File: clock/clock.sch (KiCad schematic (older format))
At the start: 3 parts, among them P101 CONN_01X03, P102 CONN_FAN_PWM, P103 XG4A-1631

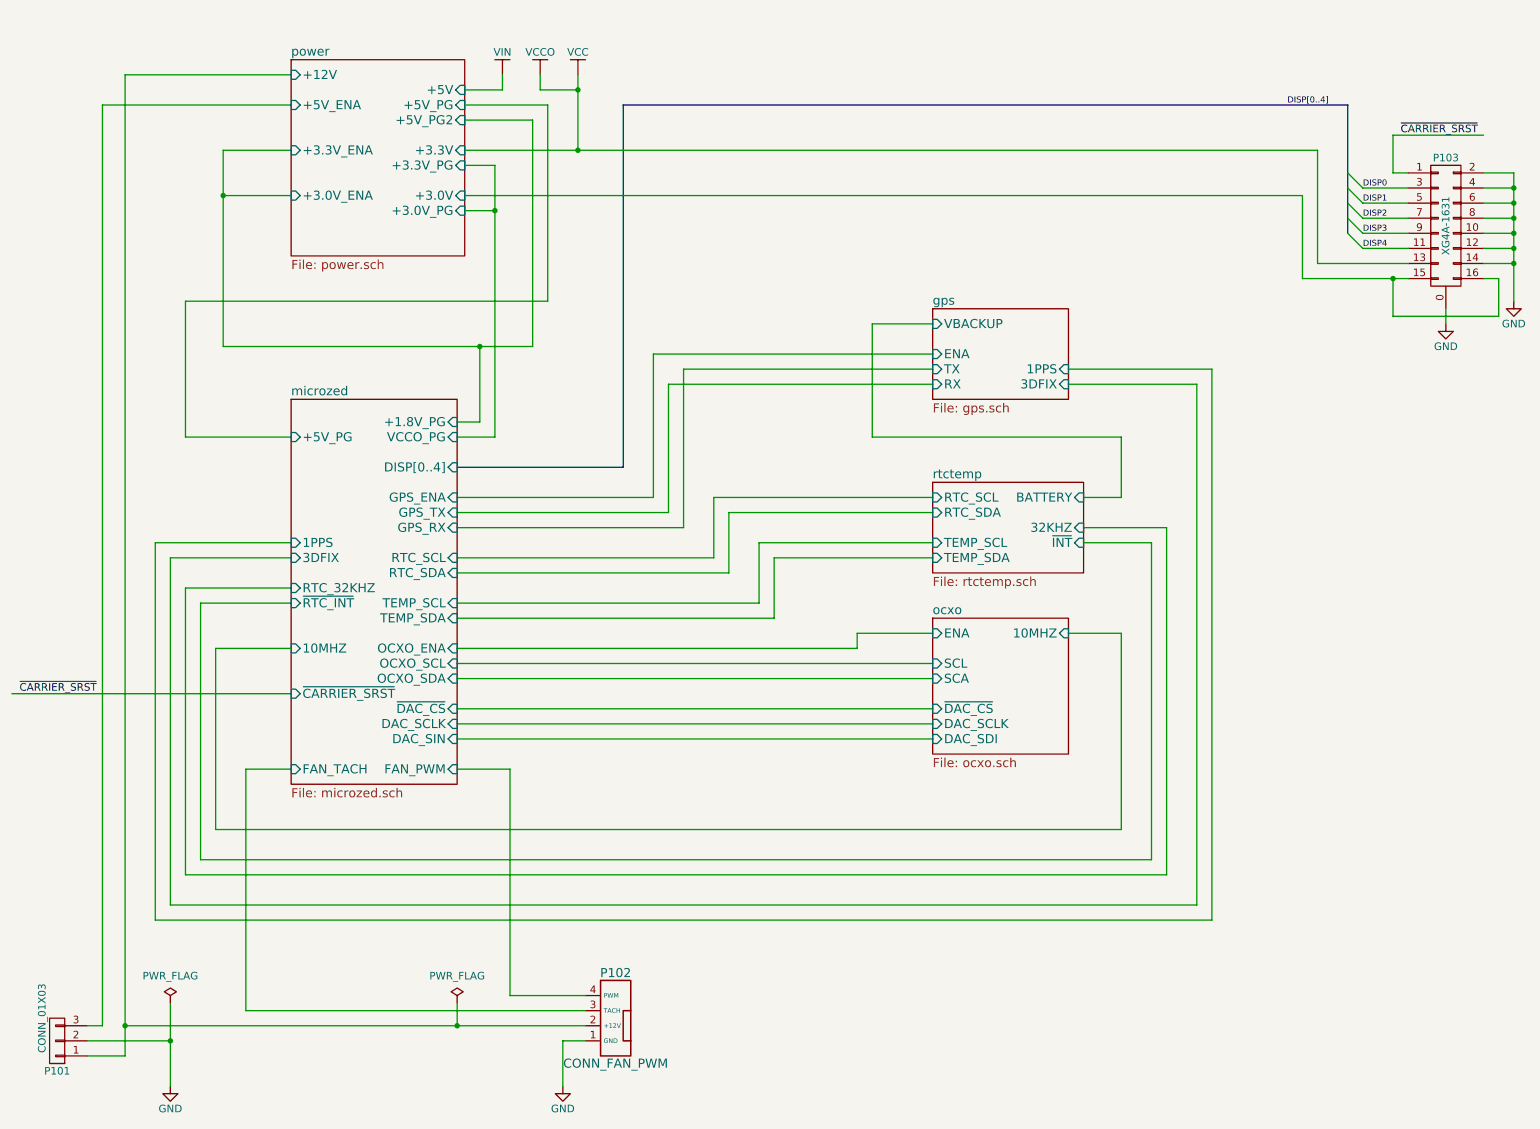
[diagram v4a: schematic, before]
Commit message: Connect temperature sensor interrupt to FPGA.
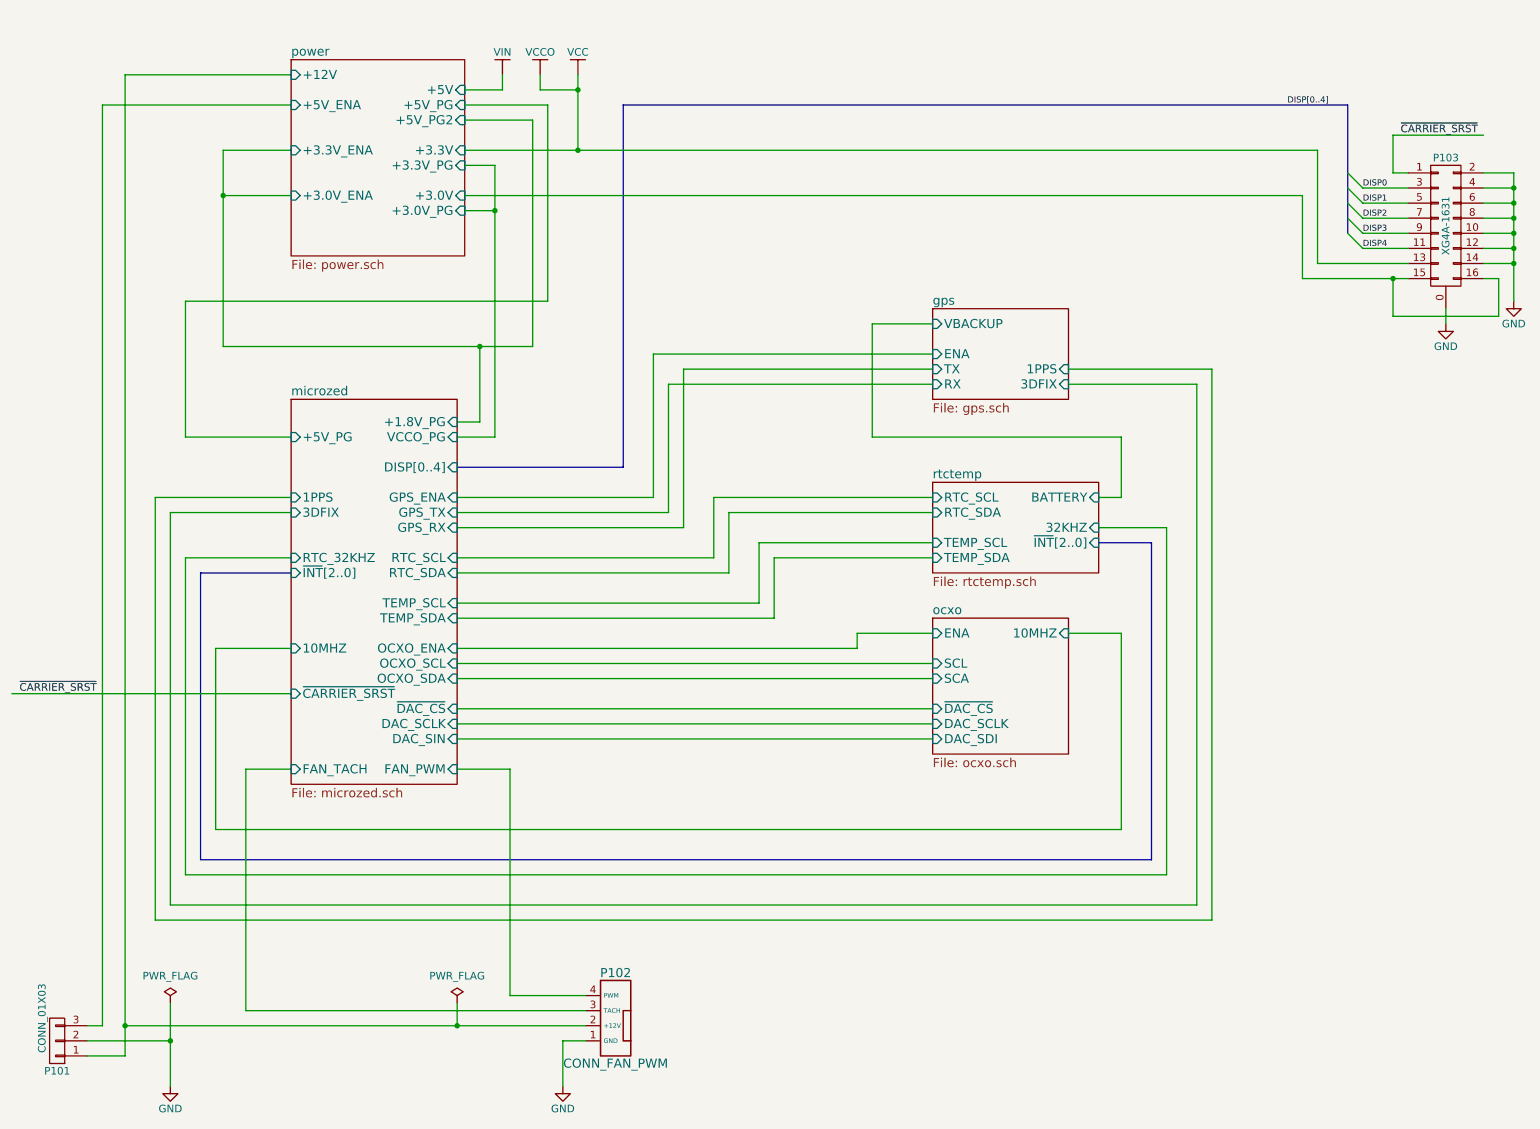
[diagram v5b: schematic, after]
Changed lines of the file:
@@
 F11 "DAC_SIN" I R 3500 5300 60
 F12 "10MHZ" I L 2400 4700 60
-F13 "1PPS" I L 2400 4000 60
-F14 "3DFIX" I L 2400 4100 60
+F13 "1PPS" I L 2400 3700 60
+F14 "3DFIX" I L 2400 3800 60
 F15 "FAN_PWM" I R 3500 5500 60
 F16 "DISP[0..4]" I R 3500 3500 60
@@
 F23 "GPS_ENA" I R 3500 3700 60
 F24 "OCXO_ENA" I R 3500 4700 60
-F25 "RTC_32KHZ" I L 2400 4300 60
-F26 "~RTC_INT~" I L 2400 4400 60
+F25 "RTC_32KHZ" I L 2400 4100 60
+F26 "~INT~[2..0]" I L 2400 4200 60
 $EndSheet
 $Sheet
@@
 $EndComp
 $Sheet
-S 6650 3600 1000 600
+S 6650 3600 1100 600
 U 5636A673
 F0 "rtctemp" 60
@@
 F2 "RTC_SCL" I L 6650 3700 60
 F3 "RTC_SDA" I L 6650 3800 60
-F4 "BATTERY" I R 7650 3700 60
+F4 "BATTERY" I R 7750 3700 60
 F5 "TEMP_SCL" I L 6650 4000 60
 F6 "TEMP_SDA" I L 6650 4100 60
-F7 "32KHZ" I R 7650 3900 60
-F8 "~INT~" I R 7650 4000 60
+F7 "32KHZ" I R 7750 3900 60
+F8 "~INT~[2..0]" I R 7750 4000 60
 $EndSheet
 Entry Wire Line
@@
 	8400 6400 1600 6400
 Wire Wire Line
-	1600 6400 1600 4100
-Wire Wire Line
-	1600 4100 2400 4100
-Wire Wire Line
-	2400 4000 1500 4000
-Wire Wire Line
-	1500 4000 1500 6500
+	1600 6400 1600 3800
+Wire Wire Line
+	1600 3800 2400 3800
+Wire Wire Line
+	2400 3700 1500 3700
+Wire Wire Line
+	1500 3700 1500 6500
 Wire Wire Line
 	1500 6500 8500 6500
@@
 	9800 2150 9200 2150
 Wire Wire Line
-	9200 2150 9200 1400
-Wire Wire Line
-	9200 1400 3550 1400
+	9200 1400 9200 2150
+Wire Wire Line
+	3550 1400 9200 1400
 Wire Wire Line
 	3500 5100 6650 5100
@@
 	5600 4100 6650 4100
 Wire Wire Line
-	7650 3700 7900 3700
+	7750 3700 7900 3700
 Wire Wire Line
 	7900 3700 7900 3300
@@
 Connection ~ 3650 2700
 Wire Wire Line
-	7650 4000 8100 4000
-Wire Wire Line
-	8100 4000 8100 6100
-Wire Wire Line
-	8100 6100 1800 6100
-Wire Wire Line
-	1800 6100 1800 4400
-Wire Wire Line
-	1800 4400 2400 4400
-Wire Wire Line
-	2400 4300 1700 4300
-Wire Wire Line
-	1700 4300 1700 6200
+	2400 4100 1700 4100
+Wire Wire Line
+	1700 4100 1700 6200
 Wire Wire Line
 	1700 6200 8200 6200
@@
 	8200 6200 8200 3900
 Wire Wire Line
-	8200 3900 7650 3900
+	8200 3900 7750 3900
 Wire Wire Line
 	5000 3900 5000 2850
@@
 Connection ~ 4300 1400
 Connection ~ 4300 1000
+Wire Bus Line
+	7750 4000 8100 4000
+Wire Bus Line
+	8100 4000 8100 6100
+Wire Bus Line
+	8100 6100 1800 6100
+Wire Bus Line
+	1800 6100 1800 4200
+Wire Bus Line
+	1800 4200 2400 4200
 $EndSCHEMATC

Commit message: Separate RTC interrupt to allow for different IO register clock domain.
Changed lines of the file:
@@
 	9800 2150 9200 2150
 Wire Wire Line
-	9200 1400 9200 2150
+	9200 2150 9200 1400
 Wire Wire Line
-	3550 1400 9200 1400
+	9200 1400 3550 1400
 Wire Wire Line
 	3500 5100 6650 5100

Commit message: Update clock board to kicad 5.1. Regenerate output files.
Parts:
- P101: symbol CONN_01X03 -> Connector_Generic:Conn_01x03
- P102: symbol CONN_FAN_PWM -> Local:CONN_FAN_PWM
- P103: symbol CONN_02X08_MTG -> Local:CONN_02X08_MTG
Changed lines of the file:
@@
-EESchema Schematic File Version 2
-LIBS:clock-rescue
-LIBS:local
-LIBS:power
-LIBS:device
-LIBS:transistors
-LIBS:conn
-LIBS:linear
-LIBS:regul
-LIBS:74xx
-LIBS:cmos4000
-LIBS:adc-dac
-LIBS:memory
-LIBS:xilinx
-LIBS:microcontrollers
-LIBS:dsp
-LIBS:microchip
-LIBS:analog_switches
-LIBS:motorola
-LIBS:texas
-LIBS:intel
-LIBS:audio
-LIBS:interface
-LIBS:digital-audio
-LIBS:philips
-LIBS:display
-LIBS:cypress
-LIBS:siliconi
-LIBS:opto
-LIBS:atmel
-LIBS:contrib
-LIBS:valves
-LIBS:clock-cache
-EELAYER 25 0
+EESchema Schematic File Version 4
+EELAYER 30 0
 EELAYER END
 $Descr A4 11693 8268
@@
 $EndSheet
 $Comp
-L GND #PWR01
+L power:GND #PWR01
 U 1 1 5632D32A
 P 10500 2400
@@
 DISP[0..4]
 $Comp
-L CONN_FAN_PWM P102
+L Local:CONN_FAN_PWM P102
 U 1 1 563D6A73
 P 4550 7150
@@
 $EndComp
 $Comp
-L GND #PWR02
+L power:GND #PWR02
 U 1 1 563D71E9
 P 4200 7600
@@
 $EndComp
 $Comp
-L CONN_01X03 P101
+L Connector_Generic:Conn_01x03 P101
 U 1 1 563D5B9B
 P 850 7300
@@
 $EndComp
 $Comp
-L GND #PWR03
+L power:GND #PWR03
 U 1 1 563D694B
 P 1600 7600
@@
 $EndComp
 $Comp
-L PWR_FLAG #FLG04
+L power:PWR_FLAG #FLG04
 U 1 1 563DBCC7
 P 1600 7050
@@
 $EndComp
 $Comp
-L PWR_FLAG #FLG05
+L power:PWR_FLAG #FLG05
 U 1 1 563DC9E1
 P 3500 7050
@@
 	4100 1100 4100 2400
 Wire Wire Line
-	1950 1400 1950 2700
+	1950 1400 1950 1700
 Wire Wire Line
 	1950 1400 2400 1400
@@
 	3550 1500 3750 1500
 Wire Wire Line
-	3750 1500 3750 3300
+	3750 1500 3750 1800
 Wire Wire Line
 	3750 3300 3500 3300
@@
 	3650 2700 3650 3200
 Wire Wire Line
-	1950 2700 4000 2700
+	1950 2700 3650 2700
 Wire Wire Line
 	4100 2400 1700 2400
@@
 	9100 1700 9100 2250
 Wire Wire Line
-	9100 2250 9800 2250
+	9100 2250 9700 2250
 Wire Wire Line
 	9800 2150 9200 2150
@@
 	9200 2150 9200 1400
 Wire Wire Line
-	9200 1400 3550 1400
+	9200 1400 4300 1400
 Wire Wire Line
 	3500 5100 6650 5100
@@
 Wire Bus Line
 	4600 1100 9400 1100
-Wire Bus Line
-	9400 1100 9400 1950
 Wire Wire Line
 	9500 1650 9800 1650
@@
 	2400 900  1300 900
 Wire Wire Line
-	1300 900  1300 7400
+	1300 900  1300 7200
 Connection ~ 1300 7200
 Wire Wire Line
 	1050 7300 1600 7300
 Wire Wire Line
-	1600 7050 1600 7600
+	1600 7050 1600 7300
 Wire Wire Line
 	3500 7050 3500 7200
@@
 Connection ~ 1600 7300
 Wire Wire Line
-	1300 7200 4350 7200
+	1300 7200 3500 7200
 Wire Wire Line
 	1300 7400 1050 7400
@@
 ~CARRIER_SRST~
 Wire Wire Line
-	10500 1550 10500 2400
+	10500 1550 10500 1650
 Wire Wire Line
 	9700 1300 10300 1300
@@
 ~CARRIER_SRST~
 $Comp
-L CONN_02X08_MTG P103
+L Local:CONN_02X08_MTG P103
 U 1 1 566653AD
 P 10050 1900
@@
 $EndComp
 $Comp
-L GND #PWR06
+L power:GND #PWR06
 U 1 1 56670FE1
 P 10050 2550
@@
 Connection ~ 9700 2250
 $Comp
-L VIN #PWR07
+L Local:VIN #PWR07
 U 1 1 5898273F
 P 3800 900
@@
 $EndComp
 $Comp
-L VCCO #PWR08
+L Local:VCCO #PWR08
 U 1 1 58982745
 P 4050 900
@@
 $EndComp
 $Comp
-L VCC #PWR09
+L Local:VCC #PWR09
 U 1 1 5898274B
 P 4300 900
@@
 	4050 1000 4300 1000
 Wire Wire Line
-	4300 900  4300 1400
+	4300 900  4300 1000
 Connection ~ 4300 1400
 Connection ~ 4300 1000
@@
 Wire Bus Line
 	1800 4200 2400 4200
+Wire Wire Line
+	1950 1700 1950 2700
+Wire Wire Line
+	3750 1800 3750 3300
+Wire Wire Line
+	10500 2150 10500 2400
+Wire Wire Line
+	10500 2050 10500 2150
+Wire Wire Line
+	10500 1950 10500 2050
+Wire Wire Line
+	10500 1850 10500 1950
+Wire Wire Line
+	10500 1750 10500 1850
+Wire Wire Line
+	1300 7200 1300 7400
+Wire Wire Line
+	3500 7200 4350 7200
+Wire Wire Line
+	1600 7300 1600 7600
+Wire Wire Line
+	10500 1650 10500 1750
+Wire Wire Line
+	3650 2700 4000 2700
+Wire Wire Line
+	9700 2250 9800 2250
+Wire Wire Line
+	4300 1400 3550 1400
+Wire Wire Line
+	4300 1000 4300 1400
+Wire Bus Line
+	9400 1100 9400 1950
 $EndSCHEMATC
